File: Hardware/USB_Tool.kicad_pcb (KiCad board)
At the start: 2 copper layers, 100 x 77 mm, 44 parts, among them J1 USB_B_Micro, J2 CONN_ICSP, J3 Extender_I2C_1, J4 Extender_I2C_2, J5 Extender_I2C_3, P1 TLMS1000, P2 150141M173100, SW1 SW_2TO1, U1 MRF89XAM8A, U2 NCP114, U3 MCP2210, U4 PIC18F46K40_44, U5 ULN2003, X1 EXTENDER_SPI_1, X2 EXTENDER_IO_1, X3 EXTENDER_IO_2, X4 EXTENDER_POWER_1, X5 EXTENDER_COM, Y1 DSC6003JI2A

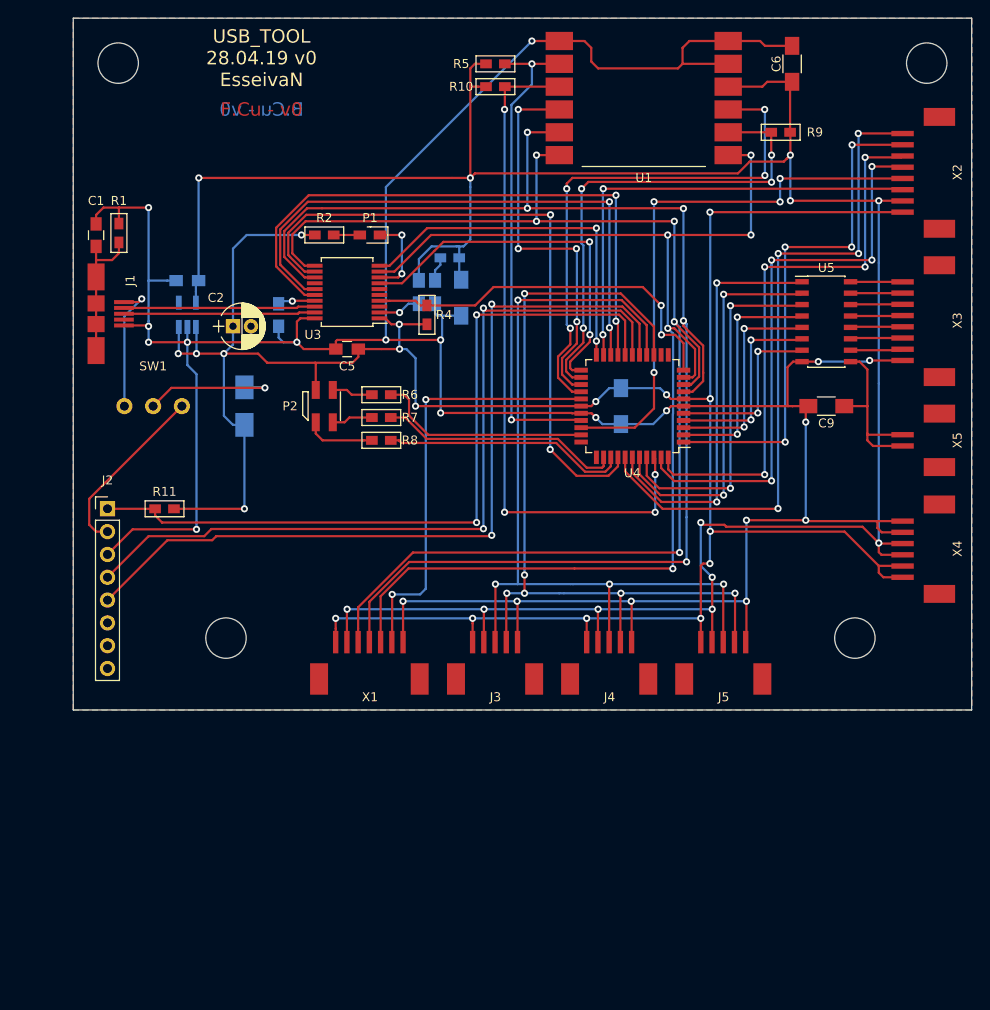
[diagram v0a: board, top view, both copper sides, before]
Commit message: v1
selectable mcu & rf transceiver power voltage
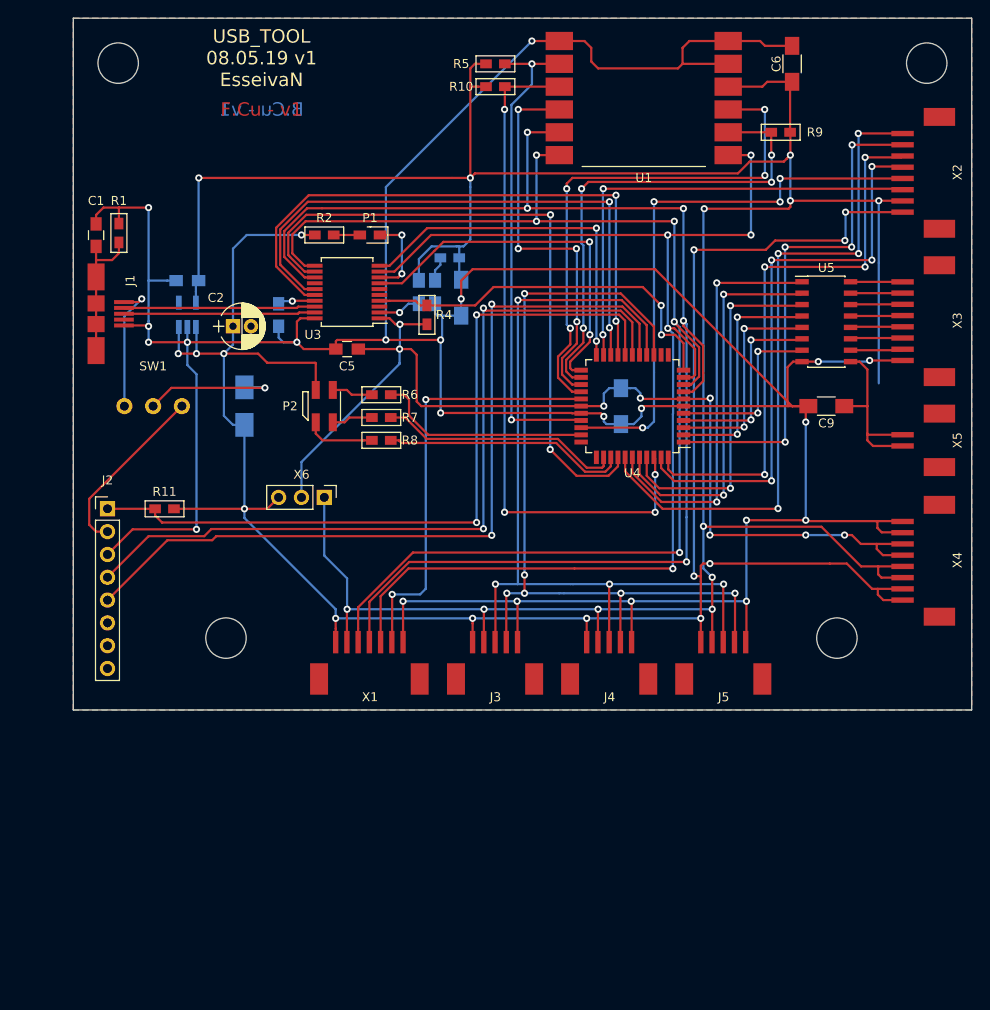
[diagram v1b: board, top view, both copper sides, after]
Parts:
- added X6: MCU_POWER_SELECT, 0EsseivaN_Lib:Pin_Header_Straight_1x03_Pitch2.54mm, F.Cu at (84.1, 94.9)
- X4: footprint 0EsseivaN_Lib:CH_06P -> 0EsseivaN_Lib:CH_08P
- moved X4 2.54 mm to (148.8, 106.4)
- moved PERC-4.5mm 2.00 mm to (141.1, 110.6)
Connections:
- C5 pad 2: 5V -> VCC
- C8 pad 1: 5V -> VCC
- J1 pad 4: (no net) -> Net-(J1-Pad4)
- J2 pad 6: (no net) -> Net-(J2-Pad6)
- J2 pad 7: (no net) -> Net-(J2-Pad7)
- J2 pad 8: (no net) -> Net-(J2-Pad8)
- R4 pad 2: 5V -> VCC
- U2 pad 4: (no net) -> Net-(U2-Pad4)
- U3 pad 1: 5V -> VCC
- U3 pad 14: (no net) -> Net-(U3-Pad14)
- U3 pad 3: (no net) -> Net-(U3-Pad3)
- U3 pad 5: (no net) -> Net-(U3-Pad5)
- U3 pad 6: (no net) -> Net-(U3-Pad6)
- U4 pad 12: (no net) -> Net-(U4-Pad12)
- U4 pad 13: (no net) -> Net-(U4-Pad13)
- U4 pad 28: 5V -> VCC
- U4 pad 33: (no net) -> Net-(U4-Pad33)
- U4 pad 34: (no net) -> Net-(U4-Pad34)
- U4 pad 7: 5V -> VCC
- X4 pad 5: GND -> VCC
- X4 pad 6: GND -> VCC
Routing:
- net VCC: track 0.00 -> 117.6 mm, vias 0 -> 8
- net GND: track 360.4 -> 410.6 mm, vias 22 -> 23
- net 3V3: track 280.4 -> 321.8 mm
- net 5V: track 279.3 -> 242.4 mm, vias 18 -> 14
- net /CLK: track 62.3 -> 63.1 mm
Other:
- board text added: "B.Cu - v1"
- board text added: "B.Mask - v1"
- board text added: "F.Cu - v1"
- board text added: "F.Mask - v1"
- board text added: "USB_TOOL 08.05.19 v1 EsseivaN"
- board text removed: "B.Cu - v0"
- board text removed: "B.Mask - v0"
- board text removed: "F.Cu - v0"
- board text removed: "F.Mask - v0"
- board text removed: "USB_TOOL 28.04.19 v0 EsseivaN"

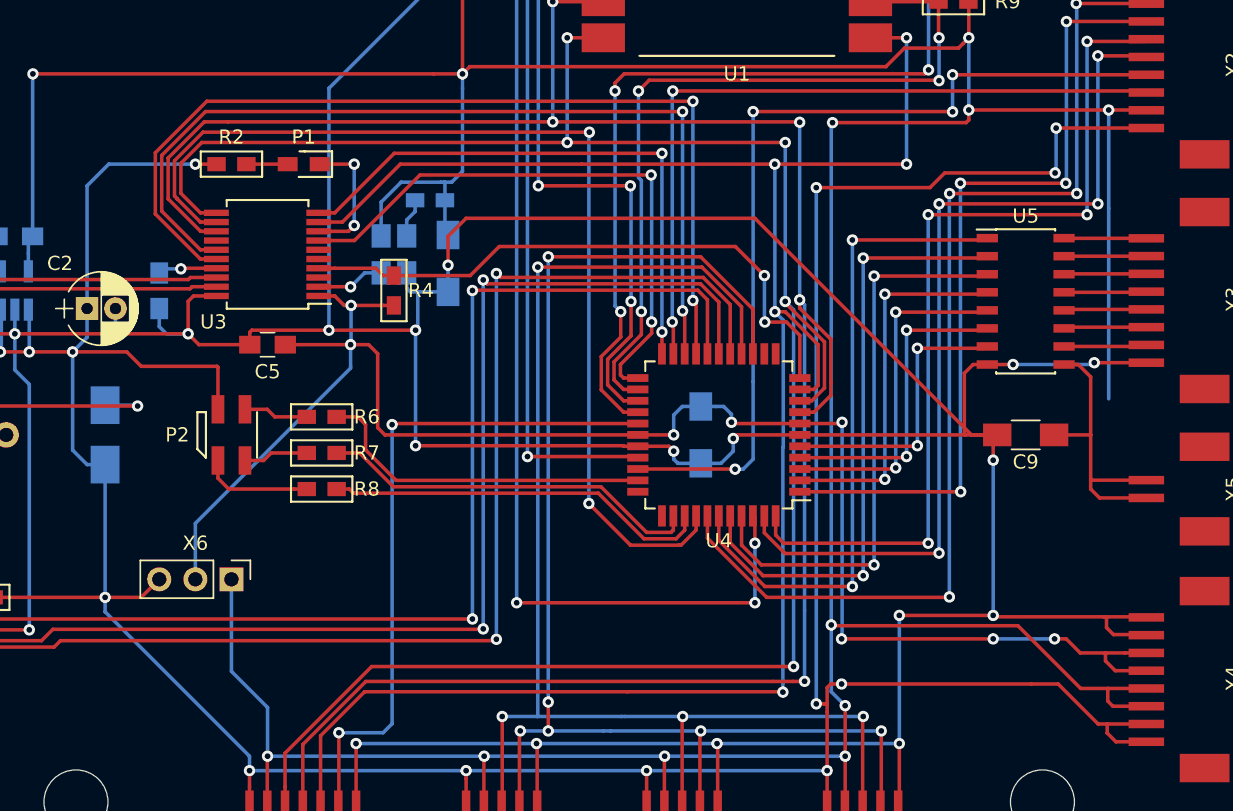
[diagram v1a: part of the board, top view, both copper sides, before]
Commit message: v2
Changed led from PORTB to PORTE
Changed IRQ0,1 & CS_EXIT to PORTB for IOC
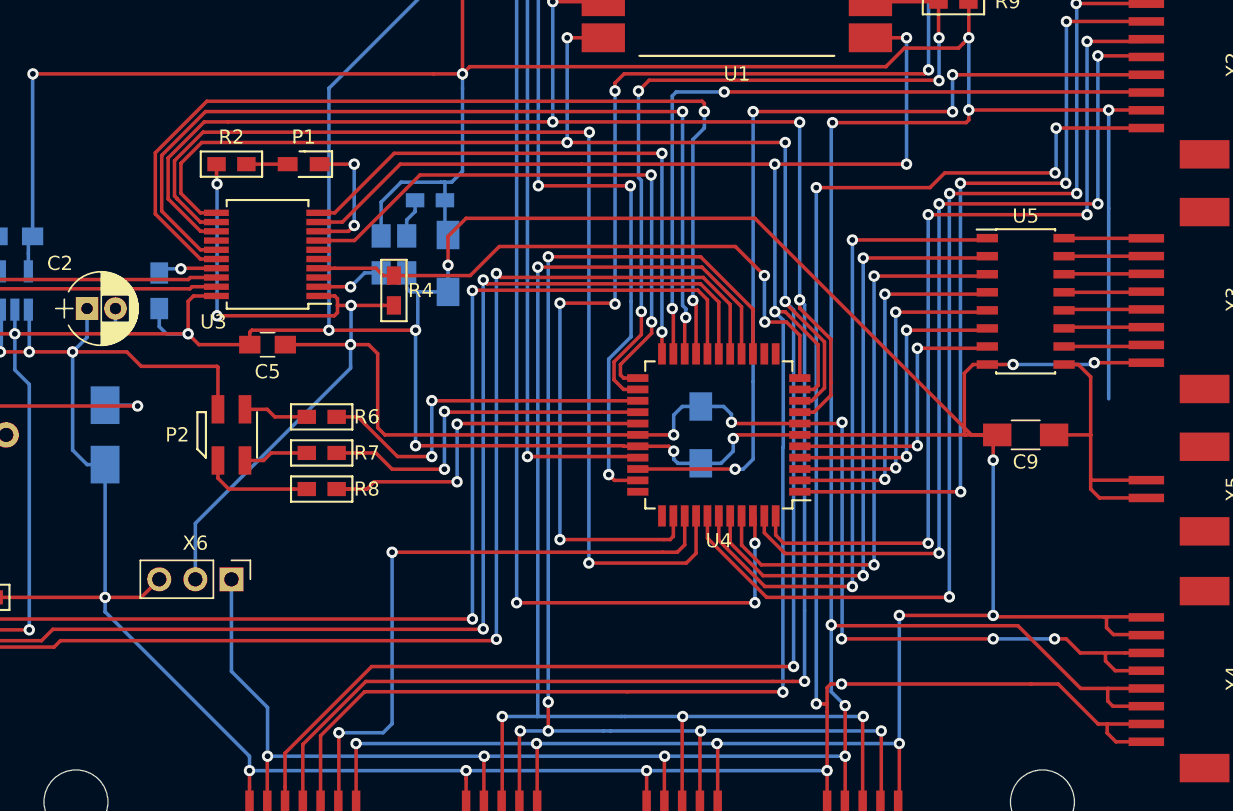
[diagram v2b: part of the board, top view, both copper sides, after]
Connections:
- net /DAC1 renamed /INT
- R2 pad 1: 5V -> VCC
- R6 pad 2: /LED_0 -> /LED_B
- R7 pad 2: /LED_1 -> /LED_G
- R8 pad 2: /LED_2 -> /LED_R
- U4 pad 25: /IRQ0 -> /LED_B
- U4 pad 26: /IRQ1 -> /LED_G
- U4 pad 27: /CS_EXT -> /LED_R
- U4 pad 32: /LED_0 -> /IRQ0
- U4 pad 35: /LED_1 -> /IRQ1
- U4 pad 36: /LED_2 -> /CS_EXT
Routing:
- net /LED_2: track 27.2 -> 0.00 mm
- net /LED_1: track 27.1 -> 0.00 mm
- net /LED_R: track 0.00 -> 26.4 mm, vias 0 -> 2
- net /LED_B: track 0.00 -> 26.3 mm, vias 0 -> 2
- net /LED_G: track 0.00 -> 25.7 mm, vias 0 -> 2
- net /LED_0: track 24.1 -> 0.00 mm
- net /IRQ1: track 59.4 -> 79.5 mm, vias 4 -> 6
- net VCC: track 117.6 -> 137.6 mm, vias 8 -> 10
- net 5V: track 242.4 -> 224.0 mm, vias 14 -> 13
- net /IRQ0: track 43.8 -> 49.7 mm
- net /~USBCFG: track 72.6 -> 77.0 mm
- net /CS_EXT: track 47.7 -> 44.2 mm
- net /BRR: track 67.1 -> 68.2 mm

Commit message: Updated silkscreen
+ mod (0/1) to 2
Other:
- board text added: "B.Cu - v2"
- board text added: "B.Mask - v2"
- board text added: "F.Cu - v2"
- board text added: "F.Mask - v2"
- board text added: "USB_TOOL 22.05.19 v2 EsseivaN"
- board text removed: "B.Cu - v1"
- board text removed: "B.Mask - v1"
- board text removed: "F.Cu - v1"
- board text removed: "F.Mask - v1"
- board text removed: "USB_TOOL 08.05.19 v1 EsseivaN"
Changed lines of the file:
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@@
   (title_block
     (title "USB Tool")
-    (date 2019-04-28)
-    (rev 0)
+    (date 2019-05-22)
+    (rev 02)
     (company ESN)
     (comment 1 "Author : EsseivaN")
@@
     (visible_elements 7FFFFFFF)
     (pcbplotparams
-      (layerselection 0x010f0_ffffffff)
+      (layerselection 0x011f0_ffffffff)
       (usegerberextensions false)
       (usegerberattributes false)
       (usegerberadvancedattributes false)
       (creategerberjobfile false)
-      (excludeedgelayer true)
+      (excludeedgelayer false)
       (linewidth 0.100000)
-      (plotframeref false)
+      (plotframeref true)
       (viasonmask false)
       (mode 1)
@@
       (padsonsilk false)
       (subtractmaskfromsilk false)
-      (outputformat 1)
+      (outputformat 4)
       (mirror false)
       (drillshape 0)
       (scaleselection 1)
-      (outputdirectory "../Fabrication/Gerber"))
+      (outputdirectory "../Fabrication/PDF"))
   )
   (net 0 "")
@@
     (arrow2b (pts (xy 56.13 19.1) (xy 57.256504 18.513579)))
   )
-  (gr_text "F.Mask - v1" (at 77.085 54.935) (layer F.Mask)
+  (gr_text "F.Mask - v2" (at 77.085 54.935) (layer F.Mask)
     (effects (font (size 1.5 1.5) (thickness 0.3)))
   )
-  (gr_text "B.Mask - v1" (at 77.085 54.935) (layer B.Mask)
+  (gr_text "B.Mask - v2" (at 77.085 54.935) (layer B.Mask)
     (effects (font (size 1.5 1.5) (thickness 0.3)) (justify mirror))
   )
-  (gr_text "B.Cu - v1" (at 77.085 51.76) (layer B.Cu)
+  (gr_text "B.Cu - v2" (at 77.085 51.76) (layer B.Cu)
     (effects (font (size 1.5 1.5) (thickness 0.3)) (justify mirror))
   )
-  (gr_text "F.Cu - v1" (at 77.085 51.76) (layer F.Cu)
+  (gr_text "F.Cu - v2" (at 77.085 51.76) (layer F.Cu)
     (effects (font (size 1.5 1.5) (thickness 0.3)))
   )
-  (gr_text "USB_TOOL\n08.05.19 v1\nEsseivaN" (at 77.085 46.045) (layer B.SilkS)
+  (gr_text "USB_TOOL\n22.05.19 v2\nEsseivaN" (at 77.085 46.045) (layer B.SilkS)
     (effects (font (size 1.5 1.5) (thickness 0.3)) (justify mirror))
   )
-  (gr_text "USB_TOOL\n08.05.19 v1\nEsseivaN" (at 77.085 46.045) (layer F.SilkS)
+  (gr_text "USB_TOOL\n22.05.19 v2\nEsseivaN" (at 77.085 46.045) (layer F.SilkS)
     (effects (font (size 1.5 1.5) (thickness 0.3)))
   )

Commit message: Some fix
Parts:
- removed C9: 100nF, 0EsseivaN_Lib:C_1206_HandSoldering
- removed J3: Extender_I2C_1, 0EsseivaN_Lib:CH_05P
- removed J4: Extender_I2C_2, 0EsseivaN_Lib:CH_05P
- removed J5: Extender_I2C_3, 0EsseivaN_Lib:CH_05P
- removed U5: ULN2003, 0EsseivaN_Lib:SOIC-16_3.9x9.9mm_Pitch1.27mm
- added R12: 1k, 0EsseivaN_Lib:R_0603_HandSoldering, F.Cu at (128.5, 103.8)
- added R13: 1k, 0EsseivaN_Lib:R_0603_HandSoldering, F.Cu at (131.1, 103.8)
- added X7: Extender_I2C_1, 0EsseivaN_Lib:CH_02P, F.Cu at (100.6, 111.5)
- added X8: Extender_I2C_2, 0EsseivaN_Lib:CH_02P, F.Cu at (112.0, 111.5)
- added X9: Extender_I2C_3, 0EsseivaN_Lib:CH_02P, F.Cu at (123.4, 111.5)
- X1: footprint 0EsseivaN_Lib:CH_07P -> 0EsseivaN_Lib:CH_04P
- X2: footprint 0EsseivaN_Lib:CH_08P -> 0EsseivaN_Lib:CH_05P
- X4: value EXTENDER_POWER_1 -> EXTENDER_POWER_2; footprint 0EsseivaN_Lib:CH_08P -> 0EsseivaN_Lib:CH_04P
- X5: value EXTENDER_COM -> EXTENDER_POWER_2; footprint 0EsseivaN_Lib:CH_02P -> 0EsseivaN_Lib:CH_04P
- moved X4 15.2 mm to (148.8, 91.1)
- moved X5 14.0 mm to (148.8, 102.6)
- moved X1 1.27 mm to (86.6, 111.5)
- moved X2 1.27 mm to (148.8, 61.9)
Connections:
- U4 pad 2: /IP4 -> /D8
- U4 pad 3: /IP5 -> /D9
- U4 pad 39: /IP1 -> /D5
- U4 pad 4: /IP6 -> /D10
- U4 pad 40: /IP2 -> /D6
- U4 pad 41: /IP3 -> /D7
- U4 pad 5: /IP7 -> /D11
- X1 pad 1: 5V -> /SCK
- X1 pad 2: 3V3 -> /MOSI
- X1 pad 3: /SCK -> /MISO
- X1 pad 4: /MOSI -> /CS_EXT
- X2 pad 1: 5V -> /INT
- X2 pad 2: 3V3 -> /CLK
- X2 pad 3: /INT -> /D1
- X2 pad 4: /CLK -> /D2
- X2 pad 5: /D1 -> /D3
- X3 pad 1: GND -> /D11
- X3 pad 2: /P1 -> /D10
- X3 pad 3: /P2 -> /D9
- X3 pad 4: /P3 -> /D8
- X3 pad 5: /P4 -> /D7
- X3 pad 6: /P5 -> /D6
- X3 pad 7: /P6 -> /D5
- X3 pad 8: /P7 -> /D4
- X4 pad 2: 5V -> 3V3
- X4 pad 3: 3V3 -> VCC
- X4 pad 4: 3V3 -> GND
- X5 pad 1: /COM -> 5V
- X5 pad 2: /COM -> 3V3
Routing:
- net GND: track 410.6 -> 273.4 mm, vias 23 -> 15
- net 3V3: track 321.8 -> 251.1 mm, vias 12 -> 10
- net 5V: track 224.0 -> 157.7 mm, vias 13 -> 7
- net /D5: track 0.00 -> 56.4 mm, vias 0 -> 2
- net /D6: track 0.00 -> 53.3 mm, vias 0 -> 2
- net /D7: track 0.00 -> 50.4 mm, vias 0 -> 2
- net /IP1: track 46.4 -> 0.00 mm, vias 2 -> 0
- net /IP2: track 43.3 -> 0.00 mm, vias 2 -> 0
- net /IP3: track 40.3 -> 0.00 mm, vias 2 -> 0
- net /D8: track 0.00 -> 36.4 mm, vias 0 -> 2
- net /D9: track 0.00 -> 34.3 mm, vias 0 -> 2
- net /D10: track 0.00 -> 32.3 mm, vias 0 -> 2
- net /D11: track 0.00 -> 30.2 mm, vias 0 -> 2
- net /IP4: track 26.3 -> 0.00 mm, vias 2 -> 0
- net /IP5: track 24.2 -> 0.00 mm, vias 2 -> 0
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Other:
- board text added: "3V3"
- board text added: "5V"
- board text added: "B.Cu - v3"
- board text added: "B.Mask - v3"
- board text added: "F.Cu - v3"
- board text added: "F.Mask - v3"
- board text added: "OFF"
- board text added: "ON"
- board text added: "USB_TOOL 01.06.19 v3 EsseivaN"
- board text added: "USB_TOOL 01.06.19 v3 Esseivan"
- board text removed: "B.Cu - v2"
- board text removed: "B.Mask - v2"
- board text removed: "F.Cu - v2"
- board text removed: "F.Mask - v2"
- board text removed: "USB_TOOL 22.05.19 v2 EsseivaN"

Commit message: v4
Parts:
- removed X6: MCU_POWER_SELECT, 0EsseivaN_Lib:Pin_Header_Straight_1x03_Pitch2.54mm
- added C9: 100nF, 0EsseivaN_Lib:C_1206_HandSoldering, F.Cu at (94.2, 58.1)
- added P3: Green, 0EsseivaN_Lib:D_0603_HandSoldering, F.Cu at (76.5, 61.9)
- added P4: Green, 0EsseivaN_Lib:D_0603_HandSoldering, F.Cu at (76.5, 59.4)
- added R14: 270R, 0EsseivaN_Lib:R_0603_HandSoldering, F.Cu at (71.4, 61.9)
- added R15: 120R, 0EsseivaN_Lib:R_0603_HandSoldering, F.Cu at (71.4, 59.4)
- C2: footprint 0EsseivaN_Lib:CP_Radial_D5.0mm_P2.00mm -> 0EsseivaN_Lib:C_0805_HandSoldering
- C3, C4, C7, C8, R3, U2, Y1: moved to F.Cu
- F1: footprint 0EsseivaN_Lib:Fuse_SMD1206_HandSoldering -> 0EsseivaN_Lib:Fuse_SMD2410_HandSoldering; moved to F.Cu
- R2: value 180R -> 150R
- R4: value 1k -> 10k
- X4, X5: footprint 0EsseivaN_Lib:CH_04P -> 0EsseivaN_Lib:CH_03P
- moved R4 18.2 mm to (87.9, 58.1), turned to 180 degrees
- moved P1 15.5 mm to (76.5, 56.8)
- moved R2 15.5 mm to (71.4, 56.8)
- moved C8 11.7 mm to (114.5, 96.2), turned to 0 degrees
- moved U2 7.62 mm to (68.8, 67.0), turned to 0 degrees
- moved C2 7.18 mm to (68.8, 70.8)
- moved C7 6.35 mm to (73.9, 67.0), turned to 270 degrees
- moved P2 3.81 mm to (87.9, 84.8)
- moved F1 2.84 mm to (77.7, 86.0), turned to 270 degrees
- moved R6 2.54 mm to (93.0, 83.5)
- moved R7 2.54 mm to (93.0, 86.0)
- moved R8 2.54 mm to (93.0, 88.6)
- moved C4 2.52 mm to (79.0, 77.2)
- moved C3 0.63 mm to (99.3, 73.3)
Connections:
- C4 pad 1: Net-(C4-Pad1) -> 3V3
- C5 pad 2: VCC -> 3V3
- C8 pad 1: VCC -> 3V3
- R12 pad 2: 5V -> 3V3
- R13 pad 2: 5V -> 3V3
- R2 pad 1: VCC -> 3V3
- R4 pad 2: VCC -> 3V3
- U3 pad 1: VCC -> 3V3
- U3 pad 17: Net-(C4-Pad1) -> 3V3
- U4 pad 28: VCC -> 3V3
- U4 pad 7: VCC -> 3V3
- X4 pad 3: VCC -> GND
- X5 pad 3: VCC -> GND
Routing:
- net VCC: track 146.6 -> 0.00 mm, vias 12 -> 0
- net 3V3: track 251.1 -> 350.9 mm, vias 10 -> 19
- net GND: track 273.4 -> 326.7 mm, vias 15 -> 16
- net /SPI_LED: track 9.41 -> 30.2 mm
- net /RESET_USB: track 42.4 -> 59.7 mm, vias 2 -> 3
- net 5V: track 157.7 -> 169.0 mm, vias 7 -> 10
- net Net-(C1-Pad2): track 15.7 -> 7.46 mm
- net /LED_B: track 26.3 -> 19.1 mm, vias 2 -> 0
- net /LED_G: track 25.7 -> 19.8 mm, vias 2 -> 0
- net /LED_R: track 26.4 -> 20.6 mm, vias 2 -> 0
- net /~SSPND: track 41.6 -> 35.8 mm, vias 2 -> 4
- net /~CSCON: track 76.4 -> 81.3 mm
- net Net-(U3-Pad2): track 4.80 -> 9.54 mm, vias 1 -> 2
- net Net-(C4-Pad1): track 4.16 -> 0.00 mm, vias 1 -> 0
- net /VBus: track 14.9 -> 18.8 mm, vias 1 -> 2
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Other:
- board text added: "B.Cu - v4"
- board text added: "B.Mask - v4"
- board text added: "F.Cu - v4"
- board text added: "F.Mask - v4"
- board text added: "USB_TOOL 17.06.19 v4 EsseivaN"
- board text added: "USB_TOOL 17.06.19 v4 Esseivan"
- board text removed: "3V3"
- board text removed: "5V"
- board text removed: "B.Cu - v3"
- board text removed: "B.Mask - v3"
- board text removed: "F.Cu - v3"
- board text removed: "F.Mask - v3"
- board text removed: "USB_TOOL 01.06.19 v3 EsseivaN"
- board text removed: "USB_TOOL 01.06.19 v3 Esseivan"
